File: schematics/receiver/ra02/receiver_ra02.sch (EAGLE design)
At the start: 47 parts, among them IC1 ATMEGA328P, Q1 16MHz, Q2 BC817-16SMD, U2 AMS1117_3.3, U3 RA-02_LORA_MODULE

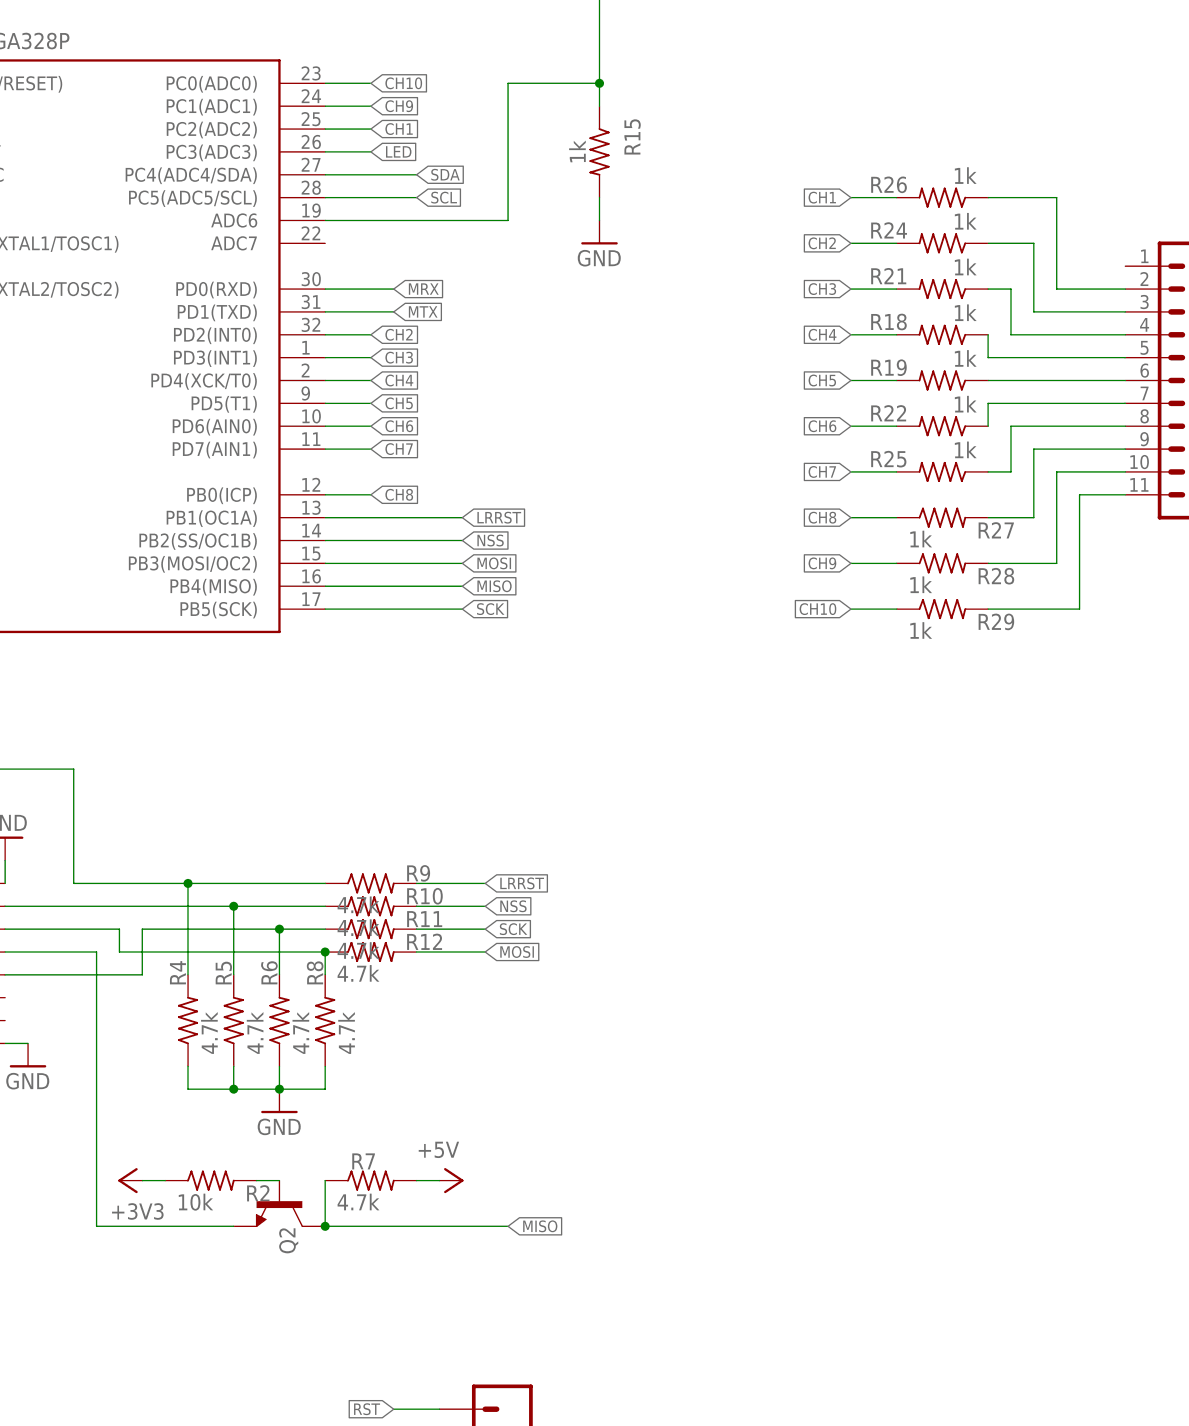
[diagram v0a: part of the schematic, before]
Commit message: Fixed incorrect resistor values.
- Fixed incorrect resistor values in the level shifters.
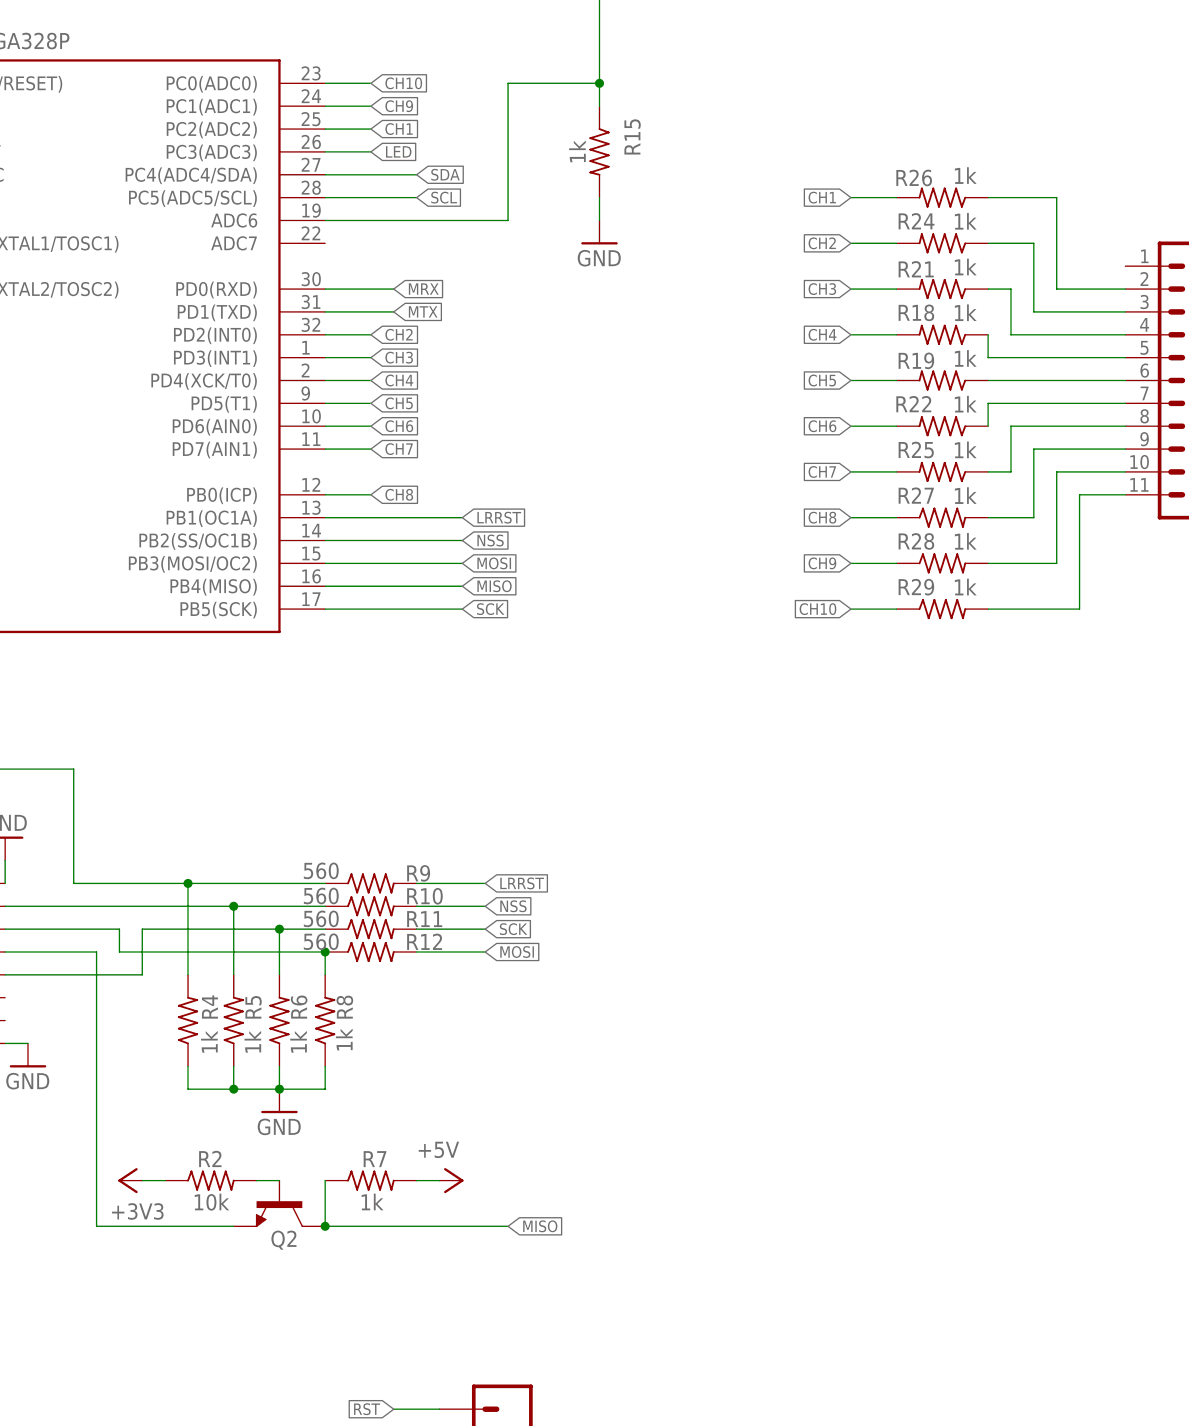
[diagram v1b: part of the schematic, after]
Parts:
- R10, R11, R12, R9: value 4.7k -> 560
- R4, R5, R6, R7, R8: value 4.7k -> 1k
